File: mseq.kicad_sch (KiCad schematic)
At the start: 66 parts, among them J1 Screen_I2C, J2 TC2030-NL, P1 USB_C_Plug_USB2.0, SW1 RESET, SW2 ON/OFF, SW3 MS/SLAVE, SW4 BOOT, U1 SN74AHCT125DR, U2 H11L1M, U3 MCP1703Ax-330xxTT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

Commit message: Almost done
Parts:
- R14: LCSC C3009719 -> C865310; MPN CRCW080522K1FKEAC -> RT0805BRD0722K1L
- R15: LCSC C844568 -> C23061; MPN CRCW060347K5FKEA -> 0603WAF4752T5E
- R16: LCSC C4141285 -> C21190; MPN CRCW06031K00FKEE -> 0603WAF1001T5E
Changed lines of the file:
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@@
 			)
 		)
-		(property "MPN" "CRCW06031K00FKEE"
+		(property "MPN" "0603WAF1001T5E"
 			(at 367.03 63.5 0)
 			(effects
@@
 			)
 		)
-		(property "LCSC" "C4141285"
+		(property "LCSC" "C21190"
 			(at 367.03 63.5 0)
 			(effects
@@
 			)
 		)
-		(property "MPN" "CRCW060347K5FKEA"
+		(property "MPN" "0603WAF4752T5E"
 			(at 345.44 88.9 0)
 			(effects
@@
 			)
 		)
-		(property "LCSC" "C844568"
+		(property "LCSC" "C23061"
 			(at 345.44 88.9 0)
 			(effects
@@
 			)
 		)
-		(property "MPN" "CRCW080522K1FKEAC"
+		(property "MPN" "RT0805BRD0722K1L"
 			(at 345.44 78.74 0)
 			(effects
@@
 			)
 		)
-		(property "LCSC" "C3009719"
+		(property "LCSC" "C865310"
 			(at 345.44 78.74 0)
 			(effects

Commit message: USB connector changed
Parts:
- P1: footprint Connector_USB:USB_C_Receptacle_GCT_USB4085 -> Connector_USB:USB_C_Receptacle_HRO_TYPE-C-31-M-12; LCSC C7095263 -> C165948; MPN USB4085-GF-A -> TYPE-C-31-M-12
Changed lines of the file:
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@@
 		)
 		(instances
-			(project ""
+			(project "mseq"
 				(path "/4f5593bf-962d-4fa9-909b-449bd6b94d0f"
 					(reference "U2")
@@
 		)
 		(instances
-			(project ""
+			(project "mseq"
 				(path "/4f5593bf-962d-4fa9-909b-449bd6b94d0f"
 					(reference "R11")
@@
 		)
 		(instances
-			(project ""
+			(project "mseq"
 				(path "/4f5593bf-962d-4fa9-909b-449bd6b94d0f"
 					(reference "#PWR09")
@@
 			)
 		)
-		(property "Footprint" "Connector_USB:USB_C_Receptacle_GCT_USB4085"
+		(property "Footprint" "Connector_USB:USB_C_Receptacle_HRO_TYPE-C-31-M-12"
 			(at 34.29 247.65 0)
 			(effects
@@
 			)
 		)
-		(property "MPN" "USB4085-GF-A"
+		(property "MPN" "TYPE-C-31-M-12"
 			(at 30.48 247.65 0)
 			(effects
@@
 			)
 		)
-		(property "LCSC" "C7095263"
+		(property "LCSC" "C165948"
 			(at 30.48 247.65 0)
 			(effects
@@
 		)
 		(instances
-			(project ""
+			(project "mseq"
 				(path "/4f5593bf-962d-4fa9-909b-449bd6b94d0f"
 					(reference "P1")
@@
 		)
 		(instances
-			(project ""
+			(project "mseq"
 				(path "/4f5593bf-962d-4fa9-909b-449bd6b94d0f"
 					(reference "Y1")
@@
 		)
 		(instances
-			(project ""
+			(project "mseq"
 				(path "/4f5593bf-962d-4fa9-909b-449bd6b94d0f"
 					(reference "#PWR011")
@@
 		)
 		(instances
-			(project ""
+			(project "mseq"
 				(path "/4f5593bf-962d-4fa9-909b-449bd6b94d0f"
 					(reference "R16")
@@
 		)
 		(instances
-			(project ""
+			(project "mseq"
 				(path "/4f5593bf-962d-4fa9-909b-449bd6b94d0f"
 					(reference "U1")
@@
 		)
 		(instances
-			(project ""
+			(project "mseq"
 				(path "/4f5593bf-962d-4fa9-909b-449bd6b94d0f"
 					(reference "D2")
@@
 		)
 		(instances
-			(project ""
+			(project "mseq"
 				(path "/4f5593bf-962d-4fa9-909b-449bd6b94d0f"
 					(reference "#PWR018")
@@
 		)
 		(instances
-			(project ""
+			(project "mseq"
 				(path "/4f5593bf-962d-4fa9-909b-449bd6b94d0f"
 					(reference "U3")
@@
 		)
 		(instances
-			(project ""
+			(project "mseq"
 				(path "/4f5593bf-962d-4fa9-909b-449bd6b94d0f"
 					(reference "U4")
@@
 		)
 		(instances
-			(project ""
+			(project "mseq"
 				(path "/4f5593bf-962d-4fa9-909b-449bd6b94d0f"
 					(reference "SW2")
@@
 		)
 		(instances
-			(project ""
+			(project "mseq"
 				(path "/4f5593bf-962d-4fa9-909b-449bd6b94d0f"
 					(reference "D1")
@@
 		)
 		(instances
-			(project ""
+			(project "mseq"
 				(path "/4f5593bf-962d-4fa9-909b-449bd6b94d0f"
 					(reference "U1")
@@
 		)
 		(instances
-			(project ""
+			(project "mseq"
 				(path "/4f5593bf-962d-4fa9-909b-449bd6b94d0f"
 					(reference "FB6")
@@
 		)
 		(instances
-			(project ""
+			(project "mseq"
 				(path "/4f5593bf-962d-4fa9-909b-449bd6b94d0f"
 					(reference "U1")
@@
 		)
 		(instances
-			(project ""
+			(project "mseq"
 				(path "/4f5593bf-962d-4fa9-909b-449bd6b94d0f"
 					(reference "D3")
@@
 		)
 		(instances
-			(project ""
+			(project "mseq"
 				(path "/4f5593bf-962d-4fa9-909b-449bd6b94d0f"
 					(reference "#PWR024")
@@
 		)
 		(instances
-			(project ""
+			(project "mseq"
 				(path "/4f5593bf-962d-4fa9-909b-449bd6b94d0f"
 					(reference "MIDI_IN1")
@@
 		)
 		(instances
-			(project ""
+			(project "mseq"
 				(path "/4f5593bf-962d-4fa9-909b-449bd6b94d0f"
 					(reference "U1")
@@
 		)
 		(instances
-			(project ""
+			(project "mseq"
 				(path "/4f5593bf-962d-4fa9-909b-449bd6b94d0f"
 					(reference "#PWR04")
@@
 		)
 		(instances
-			(project ""
+			(project "mseq"
 				(path "/4f5593bf-962d-4fa9-909b-449bd6b94d0f"
 					(reference "J2")
@@
 		)
 		(instances
-			(project ""
+			(project "mseq"
 				(path "/4f5593bf-962d-4fa9-909b-449bd6b94d0f"
 					(reference "U5")
@@
 		)
 		(instances
-			(project ""
+			(project "mseq"
 				(path "/4f5593bf-962d-4fa9-909b-449bd6b94d0f"
 					(reference "U1")
@@
 		)
 		(instances
-			(project ""
+			(project "mseq"
 				(path "/4f5593bf-962d-4fa9-909b-449bd6b94d0f"
 					(reference "J1")

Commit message: WIP, need to make the board bigger
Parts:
- D3: footprint LED_SMD:LED_PLCC-2_3.4x3.0mm_KA -> LED_SMD:LED_0603_1608Metric; LCSC C5447663 -> C375576; MPN AA4040LZGCKT-AMT -> E6Q0603VGAC1UDA
- D4, D5: footprint LED_SMD:LED_PLCC-2_3.4x3.0mm_KA -> LED_SMD:LED_0603_1608Metric; LCSC C5571318 -> C375575; MPN AA4040LQBS/D-AMT -> E6Q0603QBAC1UDA
- SW2, SW3: footprint mseq_lib:SK-12E12-G5 -> Button_Switch_THT:SW_Slide_SPDT_Angled_CK_OS102011MA1Q; LCSC C136720 -> C221530; MPN SK-12E12-G5 -> OS102011MA1QS1
- Y2: value 25MHz 9pF -> 25MHz 18pF; footprint mseq_lib:XRCGB25M000F1SBJR0 -> Crystal:Crystal_SMD_5032-2Pin_5.0x3.2mm; LCSC C26829317 -> C148312; MPN XRCGB25M000F1SBJR0 -> ABM3-25.000MHZ-D2Y-T
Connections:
- net PH0: now also Y2.2; no longer Y2.3
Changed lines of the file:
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@@
 			)
 		)
-		(property "Footprint" "mseq_lib:SK-12E12-G5"
+		(property "Footprint" "Button_Switch_THT:SW_Slide_SPDT_Angled_CK_OS102011MA1Q"
 			(at 64.77 173.99 0)
 			(effects
@@
 			)
 		)
-		(property "Datasheet" "https://www.nidec-components.com/e/catalog/switch/cas.pdf"
+		(property "Datasheet" ""
 			(at 64.77 171.45 0)
 			(effects
@@
 			)
 		)
-		(property "MPN" "SK-12E12-G5"
+		(property "MPN" "OS102011MA1QS1"
 			(at 64.77 163.83 0)
 			(effects
@@
 			)
 		)
-		(property "LCSC" "C136720"
+		(property "LCSC" "C221530"
 			(at 64.77 163.83 0)
 			(effects
@@
 	)
 	(symbol
-		(lib_name "Crystal_1")
 		(lib_id "Device:Crystal")
 		(at 213.36 257.81 90)
@@
 			)
 		)
-		(property "Value" "25MHz 9pF"
+		(property "Value" "25MHz 18pF"
 			(at 217.17 259.0799 90)
 			(effects
@@
 			)
 		)
-		(property "Footprint" "mseq_lib:XRCGB25M000F1SBJR0"
+		(property "Footprint" "Crystal:Crystal_SMD_5032-2Pin_5.0x3.2mm"
 			(at 217.424 258.318 0)
 			(effects
@@
 			)
 		)
-		(property "MPN" "XRCGB25M000F1SBJR0"
+		(property "MPN" "ABM3-25.000MHZ-D2Y-T"
 			(at 213.36 257.81 90)
 			(effects
@@
 			)
 		)
-		(property "LCSC" "C26829317"
+		(property "LCSC" "C148312"
 			(at 213.36 257.81 90)
 			(effects
@@
 		(pin "1"
 		)
-		(pin "3"
+		(pin "2"
 		)
 		(instances
@@
 			)
 		)
-		(property "Footprint" "mseq_lib:SK-12E12-G5"
+		(property "Footprint" "Button_Switch_THT:SW_Slide_SPDT_Angled_CK_OS102011MA1Q"
 			(at 52.07 242.57 0)
 			(effects
@@
 			)
 		)
-		(property "Datasheet" "https://www.nidec-components.com/e/catalog/switch/cas.pdf"
+		(property "Datasheet" ""
 			(at 52.07 240.03 0)
 			(effects
@@
 			)
 		)
-		(property "MPN" "SK-12E12-G5"
+		(property "MPN" "OS102011MA1QS1"
 			(at 52.07 232.41 0)
 			(effects
@@
 			)
 		)
-		(property "LCSC" "C136720"
+		(property "LCSC" "C221530"
 			(at 52.07 232.41 0)
 			(effects
@@
 			)
 		)
-		(property "Footprint" "LED_SMD:LED_PLCC-2_3.4x3.0mm_KA"
+		(property "Footprint" "LED_SMD:LED_0603_1608Metric"
 			(at 157.48 246.38 0)
 			(effects
@@
 			)
 		)
-		(property "Sim.Pins" "1=K 2=A"
+		(property "Sim.Pins" ""
 			(at 157.48 246.38 0)
 			(effects
@@
 			)
 		)
-		(property "MPN" "AA4040LZGCKT-AMT"
+		(property "MPN" "E6Q0603VGAC1UDA"
 			(at 157.48 246.38 0)
 			(effects
@@
 			)
 		)
-		(property "LCSC" "C5447663"
+		(property "LCSC" "C375576"
 			(at 157.48 246.38 0)
 			(effects
@@
 			)
 		)
-		(property "Footprint" "LED_SMD:LED_PLCC-2_3.4x3.0mm_KA"
+		(property "Footprint" "LED_SMD:LED_0603_1608Metric"
 			(at 157.48 257.81 0)
 			(effects
@@
 			)
 		)
-		(property "Sim.Pins" "1=K 2=A"
-			(at 157.48 257.81 0)
-			(effects
-				(font
-					(size 1.27 1.27)
-				)
-				(hide yes)
-			)
-		)
-		(property "MPN" "AA4040LQBS/D-AMT "
+		(property "MPN" "E6Q0603QBAC1UDA"
 			(at 157.48 257.81 0)
 			(effects
@@
 			)
 		)
-		(property "LCSC" "C5571318"
+		(property "LCSC" "C375575"
 			(at 157.48 257.81 0)
 			(effects
@@
 			)
 		)
-		(property "Footprint" "LED_SMD:LED_PLCC-2_3.4x3.0mm_KA"
+		(property "Footprint" "LED_SMD:LED_0603_1608Metric"
 			(at 157.48 269.24 0)
 			(effects
@@
 			)
 		)
-		(property "Sim.Pins" "1=K 2=A"
-			(at 157.48 269.24 0)
-			(effects
-				(font
-					(size 1.27 1.27)
-				)
-				(hide yes)
-			)
-		)
-		(property "MPN" "AA4040LQBS/D-AMT "
+		(property "MPN" "E6Q0603QBAC1UDA"
 			(at 157.48 269.24 0)
 			(effects
@@
 			)
 		)
-		(property "LCSC" "C5571318"
+		(property "LCSC" "C375575"
 			(at 157.48 269.24 0)
 			(effects

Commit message: Moved to new version of kicad
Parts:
- Y1: value 32.768kHz 6pF -> 32.768kHz ±20ppm 6pF
- Y2: value 25MHz 18pF -> 25 MHz ±20ppm 18pF

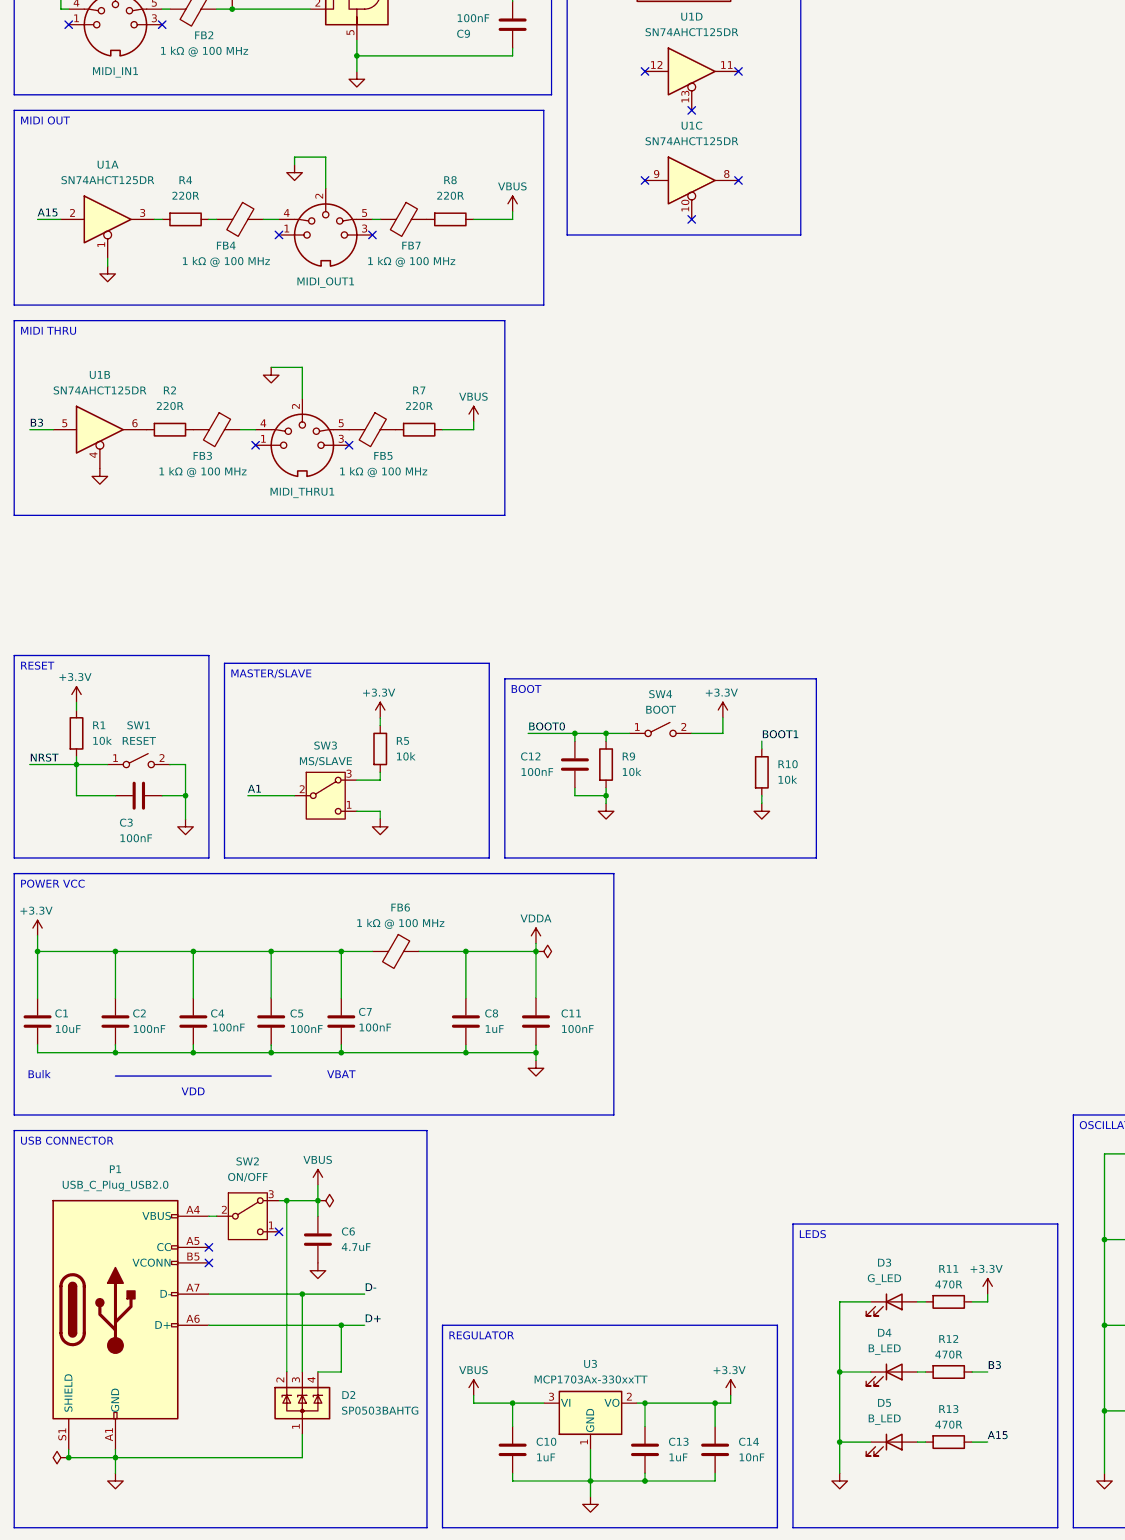
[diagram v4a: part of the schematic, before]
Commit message: LED reversed and MIDI out reversed
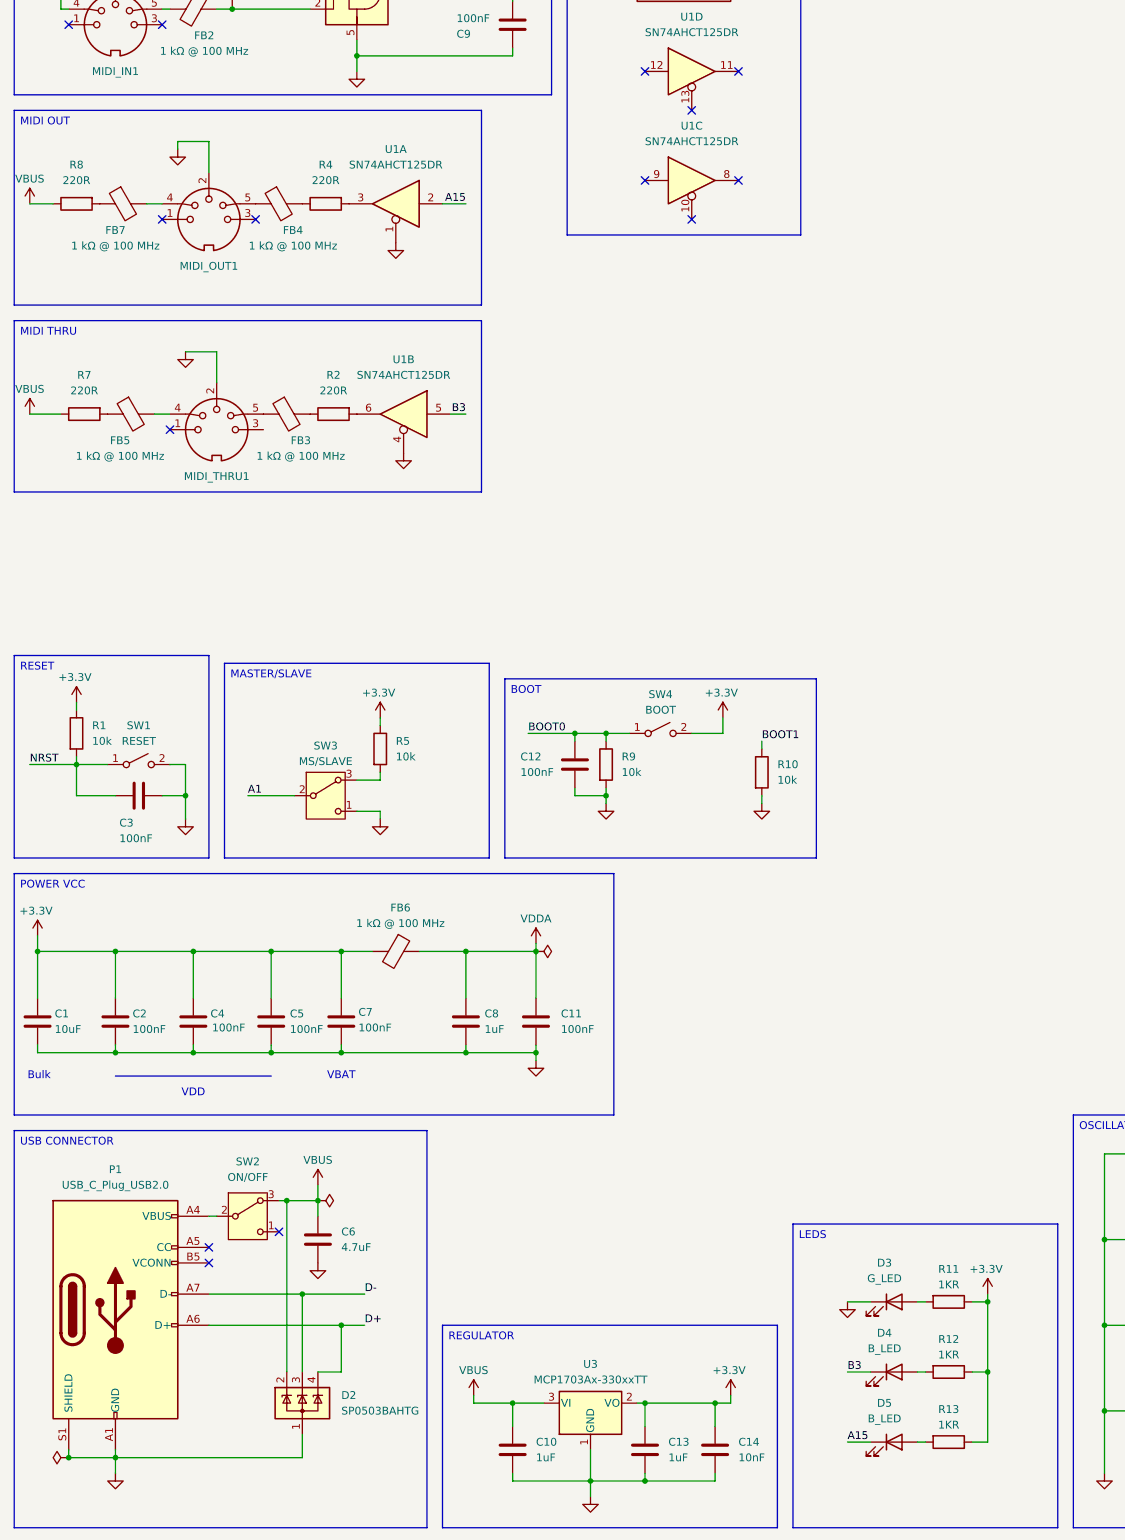
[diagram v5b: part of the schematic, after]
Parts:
- R11, R12, R13: value 470R -> 1KR; LCSC C844210 -> C17513; MPN CRCW0805470RFKEAC -> 0805W8F1001T5E
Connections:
- net +3.3V: now also R12.1, R13.1
- net A15: now also D5.1 (K); no longer R13.1
- net B3: now also D4.1 (K); no longer R12.1
- net GND: no longer D4.1 (K), D5.1 (K)
- net at MIDI_OUT1.4: now also FB7.2; no longer FB4.1
- net at MIDI_OUT1.5: now also FB4.1; no longer FB7.2
- net at FB5.2: now also MIDI_THRU1.4; no longer MIDI_THRU1.5
- net at FB3.1: now also MIDI_THRU1.5; no longer MIDI_THRU1.4
- no-connect marks 49 -> 48
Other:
- moved on the sheet: FB3, FB4, FB5, FB7, MIDI_OUT1, MIDI_THRU1, R2, R4, R7, R8, U1A, U1B

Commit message: USB bug fixed and new JTAG connector
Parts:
- removed D2: SP0503BAHTG, mseq_lib:SOT-143_4, symbol Power_Protection:SP0503BAHT
- removed J2: TC2030-NL, Connector:Tag-Connect_TC2030-IDC-NL_2x03_P1.27mm_Vertical, symbol Connector:Conn_ARM_SWD_TagConnect_TC2030-NL
- removed P1: USB_C_Plug_USB2.0, Connector_USB:USB_C_Receptacle_HRO_TYPE-C-31-M-12, symbol Connector:USB_C_Plug_USB2.0
- removed R1: 10k, Resistor_SMD:R_0603_1608Metric, symbol Device:R
- added D2: SP0505BAHT, Package_TO_SOT_SMD:SOT-23-6, symbol Power_Protection:SP0505BAHT
- added J3: Conn_ARM_JTAG_SWD_10, Connector_PinHeader_1.27mm:PinHeader_2x05_P1.27mm_Vertical_SMD, symbol Connector:Conn_ARM_JTAG_SWD_10
- added R17, R18: 5.1K, symbol Device:R
- added USB1: USB_C_Receptacle_USB2.0_16P, Connector_USB:USB_C_Receptacle_HRO_TYPE-C-31-M-12, symbol Connector:USB_C_Receptacle_USB2.0_16P
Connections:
- net +3.3V: now also J3.1 (VTref)
- net D+: now also D2.6 (K), USB1.A6 (D+), USB1.B6 (D+)
- net D-: now also D2.5 (K), USB1.A7 (D-), USB1.B7 (D-)
- net GND: now also D2.2 (A), J3.3 (GND), J3.5 (GND), J3.9 (GNDDetect), R17.2, R18.2, USB1.A1 (GND), USB1.A12 (GND), USB1.B1 (GND), USB1.B12 (GND), USB1.SH (SHIELD); no longer MIDI_OUT1.G1 (GND), MIDI_OUT1.G2 (GND), MIDI_THRU1.G1 (GND), MIDI_THRU1.G2 (GND)
- net NRST: now also J3.10 (~{RESET})
- net SWCLOCK: now also J3.4 (SWCLK/TCK)
- net SWDIO: now also J3.2 (SWDIO/TMS)
- net VBUS: now also D2.4 (K)
- net at SW2.2 (B): now also USB1.A4 (VBUS), USB1.A9 (VBUS), USB1.B4 (VBUS), USB1.B9 (VBUS)
- new net: D2.1 (K), R18.1, USB1.A5 (CC1)
- new net: D2.3 (K), R17.1, USB1.B5 (CC2)
- now unconnected: MIDI_IN1.2
- no-connect marks 48 -> 49
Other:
- note removed: "Pull-up I2C"
- moved on the sheet: C10, C13, C14, C20, C21, C6, J1, R14, R15, R16, SW2, U3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

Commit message: Second midi in added
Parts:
- added C22: 100nF, Capacitor_SMD:C_0603_1608Metric, symbol Device:C
- added D6: 1N4148, Diode_SMD:D_SOD-123, symbol Diode:1N914
- added D7: B_LED, LED_SMD:LED_0603_1608Metric, symbol Device:LED
- added FB8, FB9: 1 kΩ @ 100 MHz, Inductor_SMD:L_TDK_MLZ1608, symbol Device:FerriteBead
- added MIDI_IN2: DIN-5_180degree, mseq_lib:DIN-504, symbol Connector:DIN-5_180degree
- added R19: 220R, Resistor_SMD:R_0603_1608Metric, symbol Device:R
- added R20: 330R, Resistor_SMD:R_0603_1608Metric, symbol Device:R
- added R21: 1KR, Resistor_SMD:R_0805_2012Metric, symbol Device:R
- added U6: H11L1M, Package_DIP:SMDIP-6_W9.53mm, symbol Isolator:H11L1
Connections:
- net +3.3V: now also C22.1, R20.2, R21.1, U6.6
- net GND: now also C22.2, U6.5
- net A3: now reaches U4.13 (PA3)
- net A3: now also D7.1 (K), R20.1, U6.4
- new net: FB8.1, R19.2
- new net: FB8.2, MIDI_IN2.4
- new net: D6.1 (K), R19.1, U6.1
- new net: D6.2 (A), FB9.1, U6.2
- new net: D7.2 (A), R21.2
- new net: FB9.2, MIDI_IN2.5
- no-connect marks 49 -> 51
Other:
- moved on the sheet: C1, C11, C12, C2, C3, C4, C5, C7, C8, C9, D1, D5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
